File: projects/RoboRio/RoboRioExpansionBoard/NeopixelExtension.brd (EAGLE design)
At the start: 34 x 12.7 mm, 6 parts

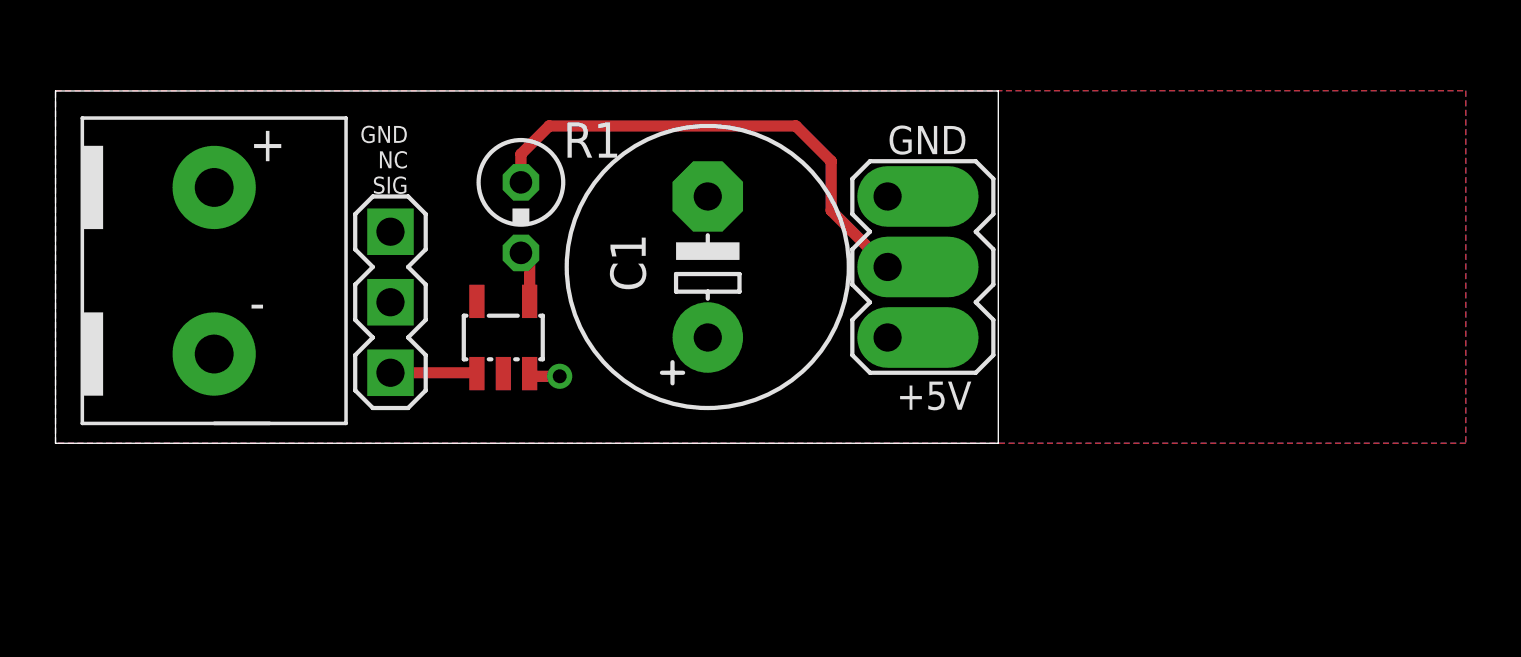
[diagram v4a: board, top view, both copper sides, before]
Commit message: Updated neopixel board
still needs to have the planes come to .025 from the board edge
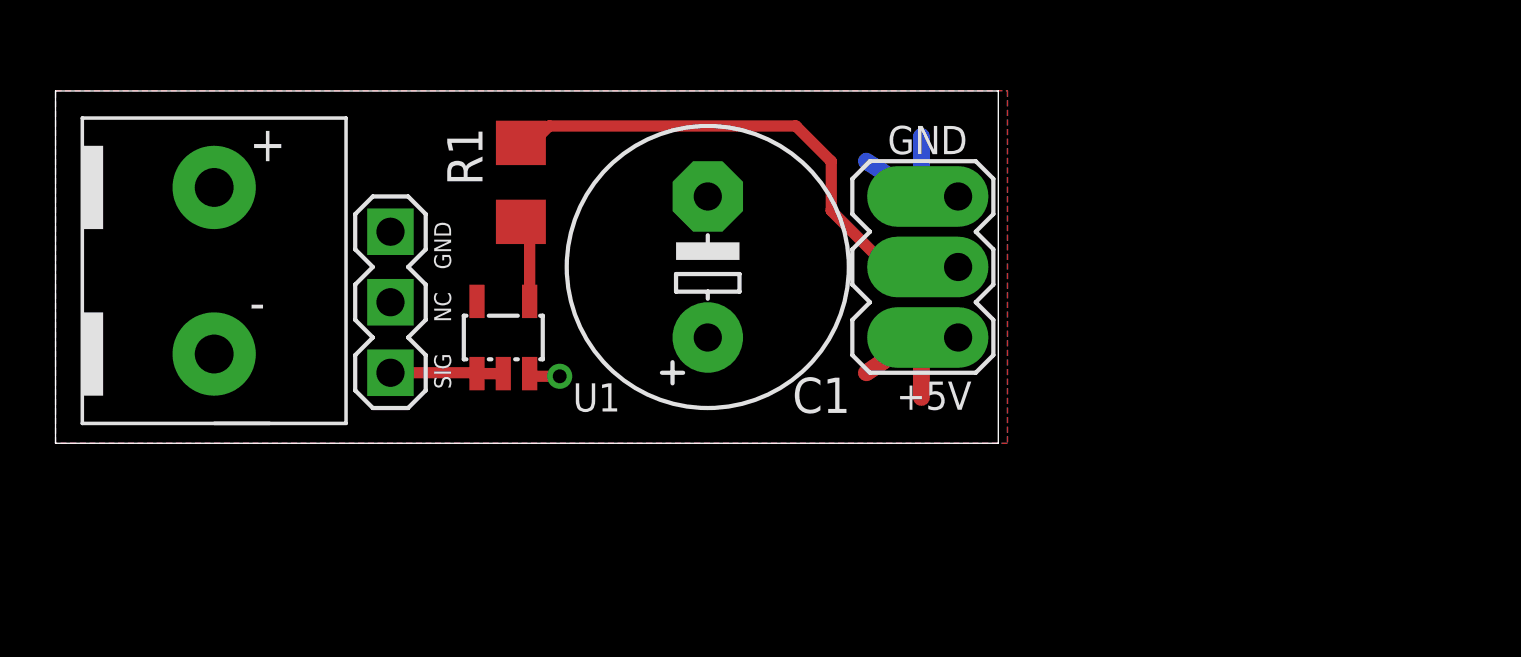
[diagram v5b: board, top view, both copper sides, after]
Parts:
- R1: device resistor:0309V -> resistor:R1206
- moved R1 1.27 mm to (16.8, 9.40)
- renumbered IN to P1, S1 to U1, U$1 to J1
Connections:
- removed net N$3: P1.3, U1.1
- new net N$2: P1.3, U1.1, U1.2
- net VCC: no longer U1.2
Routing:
- net VCC: track 0.00 -> 4.61 mm
- net N$2: track 0.00 -> 4.09 mm
- net N$1: track 17.8 -> 19.7 mm
- net N$3: track 3.14 -> 4.53 mm
- net N$4: track 1.88 -> 3.06 mm
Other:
- board text added: "+"
- board text added: "GND"
- board text added: "NC"
- board text added: "SIG"
- board text removed: "GND NC SIG"
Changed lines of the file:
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@@
 <setting verticaltext="up"/>
 </settings>
-<grid distance="0.05" unitdist="inch" unit="inch" style="lines" multiple="1" display="no" altdistance="0.005" altunitdist="inch" altunit="inch"/>
+<grid distance="0.05" unitdist="inch" unit="inch" style="lines" multiple="1" display="no" altdistance="0.0005" altunitdist="inch" altunit="inch"/>
 <layers>
 <layer number="1" name="Top" color="4" fill="1" visible="yes" active="yes"/>
@@
 <layer number="42" name="bRestrict" color="1" fill="10" visible="no" active="yes"/>
 <layer number="43" name="vRestrict" color="2" fill="10" visible="no" active="yes"/>
-<layer number="44" name="Drills" color="7" fill="1" visible="yes" active="yes"/>
-<layer number="45" name="Holes" color="7" fill="1" visible="yes" active="yes"/>
-<layer number="46" name="Milling" color="3" fill="1" visible="yes" active="yes"/>
-<layer number="47" name="Measures" color="7" fill="1" visible="yes" active="yes"/>
-<layer number="48" name="Document" color="7" fill="1" visible="yes" active="yes"/>
-<layer number="49" name="Reference" color="7" fill="1" visible="yes" active="yes"/>
+<layer number="44" name="Drills" color="7" fill="1" visible="no" active="yes"/>
+<layer number="45" name="Holes" color="7" fill="1" visible="no" active="yes"/>
+<layer number="46" name="Milling" color="3" fill="1" visible="no" active="yes"/>
+<layer number="47" name="Measures" color="7" fill="1" visible="no" active="yes"/>
+<layer number="48" name="Document" color="7" fill="1" visible="no" active="yes"/>
+<layer number="49" name="Reference" color="7" fill="1" visible="no" active="yes"/>
 <layer number="50" name="dxf" color="7" fill="1" visible="no" active="no"/>
-<layer number="51" name="tDocu" color="7" fill="1" visible="yes" active="yes"/>
-<layer number="52" name="bDocu" color="7" fill="1" visible="yes" active="yes"/>
+<layer number="51" name="tDocu" color="7" fill="1" visible="no" active="yes"/>
+<layer number="52" name="bDocu" color="7" fill="1" visible="no" active="yes"/>
 <layer number="53" name="tGND_GNDA" color="7" fill="9" visible="no" active="no"/>
 <layer number="54" name="bGND_GNDA" color="1" fill="9" visible="no" active="no"/>
@@
 <layer number="99" name="SpiceOrder" color="5" fill="1" visible="no" active="no"/>
 <layer number="100" name="Muster" color="7" fill="1" visible="no" active="no"/>
-<layer number="101" name="Patch_Top" color="12" fill="4" visible="yes" active="yes"/>
-<layer number="102" name="Vscore" color="7" fill="1" visible="yes" active="yes"/>
-<layer number="103" name="fp3" color="7" fill="1" visible="yes" active="yes"/>
-<layer number="104" name="Name" color="7" fill="1" visible="yes" active="yes"/>
+<layer number="101" name="Patch_Top" color="12" fill="4" visible="no" active="yes"/>
+<layer number="102" name="Vscore" color="7" fill="1" visible="no" active="yes"/>
+<layer number="103" name="fp3" color="7" fill="1" visible="no" active="yes"/>
+<layer number="104" name="Name" color="7" fill="1" visible="no" active="yes"/>
 <layer number="105" name="Beschreib" color="9" fill="1" visible="no" active="yes"/>
 <layer number="106" name="BGA-Top" color="4" fill="1" visible="no" active="yes"/>
@@
 <wire x1="33.96" y1="12.69" x2="0" y2="12.69" width="0" layer="20"/>
 <wire x1="0" y1="12.69" x2="0" y2="0" width="0" layer="20"/>
-<text x="12.7" y="11.43" size="0.6096" layer="25" rot="R180">GND
-NC
-SIG</text>
+<text x="13.6398" y="7.9883" size="0.6096" layer="25" rot="R270">GND</text>
+<text x="13.6398" y="5.4483" size="0.6096" layer="25" rot="R270">NC</text>
+<text x="13.6398" y="3.2385" size="0.6096" layer="25" rot="R270">SIG</text>
+<text x="10.3505" y="11.303" size="1.778" layer="27" rot="R270">+</text>
 </plain>
 <attributes>
@@
 </autorouter>
 <elements>
-<element name="R1" library="resistor" package="0309V" value="470" x="16.764" y="8.128" smashed="yes" rot="R270">
-<attribute name="NAME" x="18.288" y="10.287" size="1.27" layer="25" ratio="10"/>
-<attribute name="VALUE" x="15.1638" y="8.636" size="1.27" layer="27" ratio="10" rot="R90"/>
+<element name="R1" library="resistor" package="R1206" value="470" x="16.764" y="9.398" smashed="yes" rot="R270">
+<attribute name="NAME" x="15.3797" y="9.2837" size="1.27" layer="25" ratio="10" rot="R90"/>
 </element>
-<element name="IN" library="con-lstb-modified" package="MA03-1" value="" x="12.065" y="5.08" smashed="yes" rot="R270">
+<element name="P1" library="con-lstb-modified" package="MA03-1" value="" x="12.065" y="5.08" smashed="yes" rot="R270">
 <attribute name="OC_NEWARK" value="unknown" x="12.065" y="5.08" size="1.778" layer="27" rot="R270" display="off"/>
 <attribute name="MPN" value="" x="12.065" y="5.08" size="1.778" layer="27" rot="R270" display="off"/>
@@
 </element>
 <element name="C1" library="adafruit" package="E5-10,5" value="1000uf" x="23.495" y="6.35" smashed="yes" rot="R90">
-<attribute name="NAME" x="21.2598" y="5.461" size="1.27" layer="25" ratio="10" rot="R90"/>
-<attribute name="VALUE" x="26.7208" y="3.2258" size="1.27" layer="27" ratio="10" rot="R90"/>
+<attribute name="NAME" x="26.543" y="1.0922" size="1.27" layer="25" ratio="10"/>
 </element>
-<element name="U$1" library="Molex-39543-0002" package="POWER" value="POWER" x="5.715" y="5.715"/>
+<element name="J1" library="Molex-39543-0002" package="POWER" value="POWER" x="5.715" y="5.715" smashed="yes"/>
 <element name="U$2" library="NeopixelConnector" package="NEODIRECTSOLDERORMA03-1" value="NEOPIXEL1" x="29.972" y="6.35" smashed="yes" rot="R270"/>
-<element name="S1" library="SOT25" package="SOT25" value="74AHCT1G08" x="16.129" y="3.81" smashed="yes">
-<attribute name="VALUE" x="13.589" y="1.016" size="0.8128" layer="27"/>
+<element name="U1" library="SOT25" package="SOT25" value="74AHCT1G08" x="16.129" y="3.81" smashed="yes">
+<attribute name="NAME" x="18.6309" y="1.143" size="1.016" layer="25"/>
 </element>
 </elements>
@@
 <contactref element="R1" pad="1"/>
 <contactref element="U$2" pad="DATA"/>
-<wire x1="16.764" y1="9.398" x2="16.764" y2="10.414" width="0.4064" layer="1"/>
+<wire x1="16.764" y1="10.82" x2="16.764" y2="10.414" width="0.4064" layer="1"/>
 <wire x1="16.764" y1="10.414" x2="17.78" y2="11.43" width="0.4064" layer="1"/>
 <wire x1="17.78" y1="11.43" x2="26.67" y2="11.43" width="0.4064" layer="1"/>
@@
 <wire x1="27.94" y1="10.16" x2="27.94" y2="8.382" width="0.4064" layer="1"/>
 <wire x1="27.94" y1="8.382" x2="29.972" y2="6.35" width="0.4064" layer="1"/>
+<wire x1="29.972" y1="6.35" x2="30.48" y2="6.35" width="0.4064" layer="1"/>
+<wire x1="30.48" y1="6.35" x2="32.512" y2="6.35" width="0.4064" layer="1"/>
 </signal>
 <signal name="GND">
-<contactref element="IN" pad="1"/>
+<contactref element="P1" pad="1"/>
 <contactref element="C1" pad="-"/>
 <polygon width="0.4064" layer="16">
-<vertex x="50.8" y="12.7"/>
-<vertex x="50.8" y="0"/>
+<vertex x="34.29" y="12.7"/>
+<vertex x="34.29" y="0"/>
 <vertex x="0" y="0"/>
 <vertex x="0" y="12.7"/>
 </polygon>
-<contactref element="U$1" pad="GND"/>
+<contactref element="J1" pad="GND"/>
 <contactref element="U$2" pad="GND"/>
-<contactref element="S1" pad="3"/>
+<contactref element="U1" pad="3"/>
 <via x="18.161" y="2.413" extent="1-16" drill="0.5"/>
 <wire x1="18.161" y1="2.413" x2="17.176" y2="2.413" width="0.4064" layer="1"/>
 <wire x1="17.176" y1="2.413" x2="17.079" y2="2.51" width="0.4064" layer="1"/>
 </signal>
-<signal name="N$3">
-<contactref element="IN" pad="3"/>
-<contactref element="S1" pad="1"/>
-<wire x1="12.065" y1="2.54" x2="15.179" y2="2.54" width="0.4064" layer="1"/>
-<wire x1="15.179" y1="2.54" x2="15.179" y2="2.51" width="0.4064" layer="1"/>
-</signal>
 <signal name="N$4">
 <contactref element="R1" pad="2"/>
-<contactref element="S1" pad="4"/>
-<wire x1="17.079" y1="5.11" x2="17.079" y2="6.543" width="0.4064" layer="1"/>
-<wire x1="17.079" y1="6.543" x2="16.764" y2="6.858" width="0.4064" layer="1"/>
+<contactref element="U1" pad="4"/>
+<wire x1="17.079" y1="5.11" x2="17.079" y2="7.813" width="0.4064" layer="1"/>
+<wire x1="17.079" y1="7.813" x2="16.764" y2="7.976" width="0.4064" layer="1"/>
 </signal>
 <signal name="VCC">
 <contactref element="C1" pad="+"/>
-<contactref element="U$1" pad="5V"/>
-<polygon width="0.4064" layer="1">
+<contactref element="J1" pad="5V"/>
+<polygon width="0.6096" layer="1">
 <vertex x="0" y="12.7"/>
-<vertex x="50.8" y="12.7"/>
-<vertex x="50.8" y="0"/>
+<vertex x="34.29" y="12.7"/>
+<vertex x="34.29" y="0"/>
 <vertex x="0" y="0"/>
 </polygon>
 <contactref element="U$2" pad="5V"/>
-<contactref element="S1" pad="5"/>
-<contactref element="S1" pad="2"/>
+<contactref element="U1" pad="5"/>
+<wire x1="31.1912" y1="3.8735" x2="29.21" y2="2.54" width="0.6096" layer="1"/>
+<wire x1="31.1912" y1="3.8735" x2="31.1912" y2="1.651" width="0.6096" layer="1"/>
+</signal>
+<signal name="N$2">
+<contactref element="U1" pad="1"/>
+<contactref element="P1" pad="3"/>
+<contactref element="U1" pad="2"/>
+<wire x1="12.065" y1="2.54" x2="15.179" y2="2.54" width="0.4064" layer="1"/>
+<wire x1="15.179" y1="2.54" x2="15.179" y2="2.51" width="0.4064" layer="1"/>
+<wire x1="15.179" y1="2.51" x2="16.129" y2="2.51" width="0.4064" layer="1"/>
+</signal>
+<signal name="N$3">
+<wire x1="31.1912" y1="11.049" x2="31.1912" y2="8.8773" width="0.6096" layer="16"/>
+<wire x1="31.1912" y1="8.8773" x2="29.21" y2="10.16" width="0.6096" layer="16"/>
 </signal>
 </signals>
 </board>
 </drawing>
-<compatibility>
-<note version="6.3" minversion="6.2.2" severity="warning">
-Since Version 6.2.2 text objects can contain more than one line,
-which will not be processed correctly with this version.
-</note>
-</compatibility>
 </eagle>

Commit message: Made sure Neopixel board could be fabricated
following a new DRU for midwestpcb
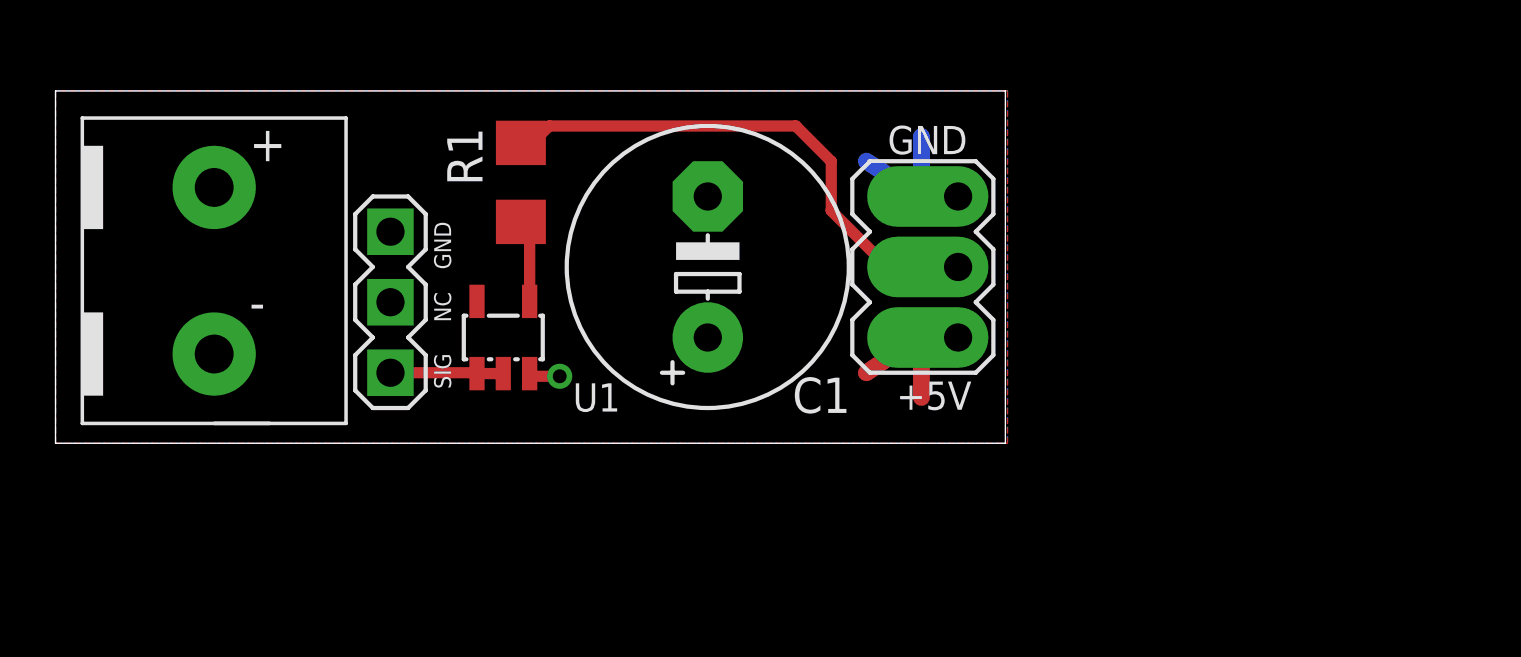
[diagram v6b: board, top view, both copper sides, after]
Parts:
- P1: value (none) -> Input
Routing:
- net N$3: track 4.53 -> 0.00 mm
- net GND: track 1.12 -> 5.65 mm
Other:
- board size 34 x 12.7 mm -> 34.2 x 12.7 mm
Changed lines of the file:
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@@
 <setting verticaltext="up"/>
 </settings>
-<grid distance="0.05" unitdist="inch" unit="inch" style="lines" multiple="1" display="no" altdistance="0.0005" altunitdist="inch" altunit="inch"/>
+<grid distance="0.05" unitdist="inch" unit="inch" style="lines" multiple="1" display="no" altdistance="0.01" altunitdist="inch" altunit="inch"/>
 <layers>
 <layer number="1" name="Top" color="4" fill="1" visible="yes" active="yes"/>
@@
 <board>
 <plain>
-<wire x1="0" y1="0" x2="33.96" y2="0" width="0" layer="20"/>
-<wire x1="33.96" y1="0" x2="33.96" y2="12.69" width="0" layer="20"/>
-<wire x1="33.96" y1="12.69" x2="0" y2="12.69" width="0" layer="20"/>
+<wire x1="0" y1="0" x2="34.214" y2="0" width="0" layer="20"/>
+<wire x1="34.214" y1="0" x2="34.214" y2="12.69" width="0" layer="20"/>
+<wire x1="34.214" y1="12.69" x2="0" y2="12.69" width="0" layer="20"/>
 <wire x1="0" y1="12.69" x2="0" y2="0" width="0" layer="20"/>
 <text x="13.6398" y="7.9883" size="0.6096" layer="25" rot="R270">GND</text>
@@
 </class>
 </classes>
-<designrules name="default">
+<designrules name="midwestpcb *">
 <description language="de">&lt;b&gt;EAGLE Design Rules&lt;/b&gt;
 &lt;p&gt;
@@
 <description language="en">&lt;b&gt;EAGLE Design Rules&lt;/b&gt;
 &lt;p&gt;
-The default Design Rules have been set to cover
-a wide range of applications. Your particular design
-may have different requirements, so please make the
-necessary adjustments and save your customized
-design rules under a new name.</description>
+These design rules are made for midwestpcb.</description>
 <param name="layerSetup" value="(1*16)"/>
 <param name="mtCopper" value="0.035mm 0.035mm 0.035mm 0.035mm 0.035mm 0.035mm 0.035mm 0.035mm 0.035mm 0.035mm 0.035mm 0.035mm 0.035mm 0.035mm 0.035mm 0.035mm"/>
 <param name="mtIsolate" value="1.5mm 0.15mm 0.2mm 0.15mm 0.2mm 0.15mm 0.2mm 0.15mm 0.2mm 0.15mm 0.2mm 0.15mm 0.2mm 0.15mm 0.2mm"/>
-<param name="mdWireWire" value="8mil"/>
-<param name="mdWirePad" value="8mil"/>
-<param name="mdWireVia" value="8mil"/>
-<param name="mdPadPad" value="8mil"/>
-<param name="mdPadVia" value="8mil"/>
-<param name="mdViaVia" value="8mil"/>
-<param name="mdSmdPad" value="8mil"/>
-<param name="mdSmdVia" value="8mil"/>
-<param name="mdSmdSmd" value="8mil"/>
+<param name="mdWireWire" value="3mil"/>
+<param name="mdWirePad" value="3mil"/>
+<param name="mdWireVia" value="3mil"/>
+<param name="mdPadPad" value="3mil"/>
+<param name="mdPadVia" value="3mil"/>
+<param name="mdViaVia" value="3mil"/>
+<param name="mdSmdPad" value="3mil"/>
+<param name="mdSmdVia" value="3mil"/>
+<param name="mdSmdSmd" value="3mil"/>
 <param name="mdViaViaSameLayer" value="8mil"/>
 <param name="mnLayersViaInSmd" value="2"/>
-<param name="mdCopperDimension" value="40mil"/>
+<param name="mdCopperDimension" value="15mil"/>
 <param name="mdDrill" value="8mil"/>
 <param name="mdSmdStop" value="0mil"/>
-<param name="msWidth" value="10mil"/>
-<param name="msDrill" value="24mil"/>
+<param name="msWidth" value="3mil"/>
+<param name="msDrill" value="6mil"/>
 <param name="msMicroVia" value="9.99mm"/>
 <param name="msBlindViaRatio" value="0.5"/>
@@
 <param name="mvStopFrame" value="1"/>
 <param name="mvCreamFrame" value="0"/>
-<param name="mlMinStopFrame" value="4mil"/>
+<param name="mlMinStopFrame" value="3mil"/>
 <param name="mlMaxStopFrame" value="4mil"/>
 <param name="mlMinCreamFrame" value="0mil"/>
@@
 <attribute name="NAME" x="15.3797" y="9.2837" size="1.27" layer="25" ratio="10" rot="R90"/>
 </element>
-<element name="P1" library="con-lstb-modified" package="MA03-1" value="" x="12.065" y="5.08" smashed="yes" rot="R270">
+<element name="P1" library="con-lstb-modified" package="MA03-1" value="Input" x="12.065" y="5.08" smashed="yes" rot="R270">
 <attribute name="OC_NEWARK" value="unknown" x="12.065" y="5.08" size="1.778" layer="27" rot="R270" display="off"/>
 <attribute name="MPN" value="" x="12.065" y="5.08" size="1.778" layer="27" rot="R270" display="off"/>
@@
 <contactref element="P1" pad="1"/>
 <contactref element="C1" pad="-"/>
-<polygon width="0.4064" layer="16">
+<polygon width="0.6096" layer="16">
 <vertex x="34.29" y="12.7"/>
 <vertex x="34.29" y="0"/>
@@
 <wire x1="18.161" y1="2.413" x2="17.176" y2="2.413" width="0.4064" layer="1"/>
 <wire x1="17.176" y1="2.413" x2="17.079" y2="2.51" width="0.4064" layer="1"/>
+<wire x1="31.1912" y1="11.049" x2="31.1912" y2="8.8773" width="0.6096" layer="16"/>
+<wire x1="31.1912" y1="8.8773" x2="29.21" y2="10.16" width="0.6096" layer="16"/>
 </signal>
 <signal name="N$4">
@@
 <contactref element="C1" pad="+"/>
 <contactref element="J1" pad="5V"/>
-<polygon width="0.6096" layer="1">
-<vertex x="0" y="12.7"/>
-<vertex x="34.29" y="12.7"/>
-<vertex x="34.29" y="0"/>
-<vertex x="0" y="0"/>
-</polygon>
 <contactref element="U$2" pad="5V"/>
 <contactref element="U1" pad="5"/>
 <wire x1="31.1912" y1="3.8735" x2="29.21" y2="2.54" width="0.6096" layer="1"/>
 <wire x1="31.1912" y1="3.8735" x2="31.1912" y2="1.651" width="0.6096" layer="1"/>
+<polygon width="0.6096" layer="1" spacing="0.6096">
+<vertex x="0" y="0"/>
+<vertex x="34.29" y="0"/>
+<vertex x="34.29" y="12.7"/>
+<vertex x="0" y="12.7"/>
+</polygon>
 </signal>
 <signal name="N$2">
@@
 <wire x1="15.179" y1="2.51" x2="16.129" y2="2.51" width="0.4064" layer="1"/>
 </signal>
-<signal name="N$3">
-<wire x1="31.1912" y1="11.049" x2="31.1912" y2="8.8773" width="0.6096" layer="16"/>
-<wire x1="31.1912" y1="8.8773" x2="29.21" y2="10.16" width="0.6096" layer="16"/>
-</signal>
 </signals>
